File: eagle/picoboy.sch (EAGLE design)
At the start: 8 parts

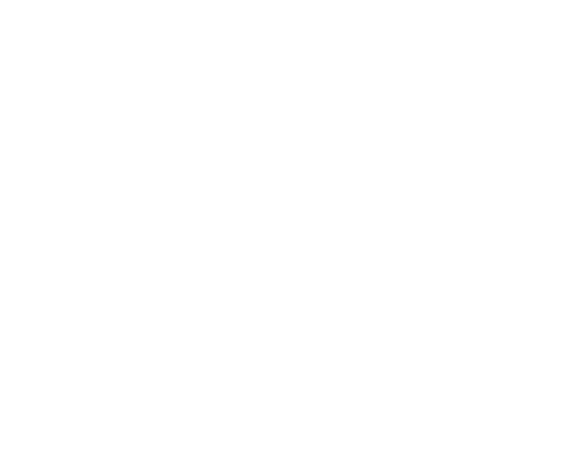
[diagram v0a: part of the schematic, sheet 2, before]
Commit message: Replace Game Boy Pocket with Game Boy Color PCB outline
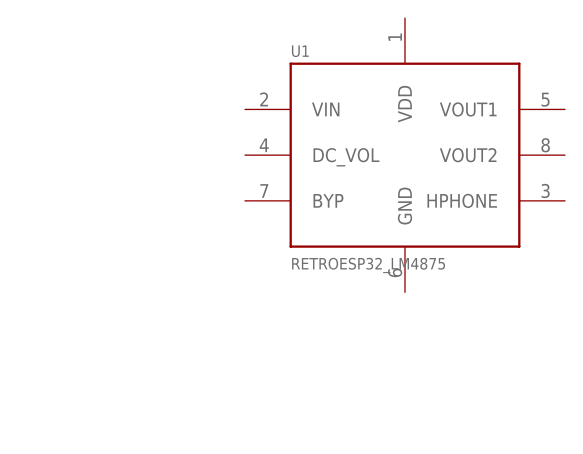
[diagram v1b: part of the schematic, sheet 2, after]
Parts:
- added U1: RETROESP32_LM4875, GabozeLite:RETROESP32_LM4875
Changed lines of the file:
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@@
 <part name="SELECT" library="GabozeLite" deviceset="RETROESP32_CONDUCTIVE_BUTTON_STARTSELECT" device="CONDUCTIVE_BUTTON_THICK_STARTSELECT"/>
 <part name="START" library="GabozeLite" deviceset="RETROESP32_CONDUCTIVE_BUTTON_STARTSELECT" device="CONDUCTIVE_BUTTON_THICK_STARTSELECT"/>
+<part name="U1" library="GabozeLite" deviceset="RETROESP32_LM4875" device=""/>
 </parts>
 <sheets>
@@
 <attribute name="NAME" x="76.2" y="151.13" size="1.9304" layer="95" font="vector" ratio="20" align="center"/>
 </instance>
+<instance part="U1" gate="U$1" x="182.88" y="162.56" smashed="yes">
+<attribute name="NAME" x="177.8" y="173.482" size="1.27" layer="95"/>
+<attribute name="VALUE" x="177.8" y="149.86" size="1.27" layer="96"/>
+</instance>
 </instances>

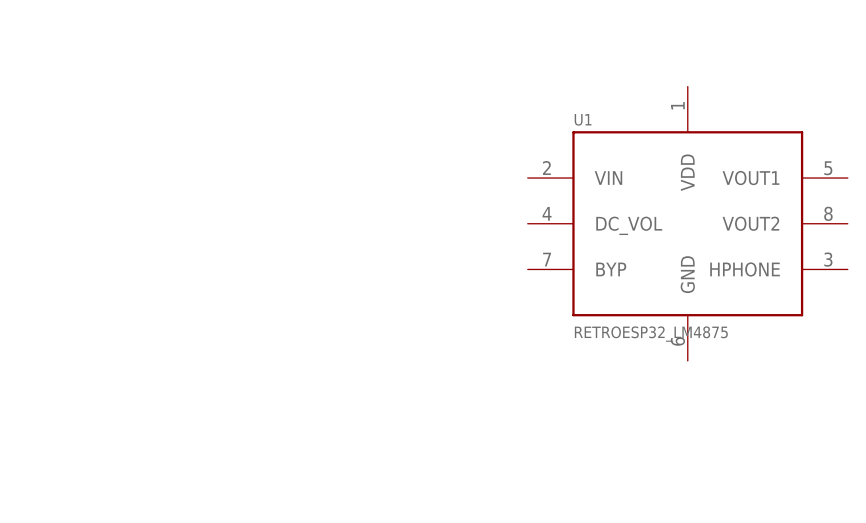
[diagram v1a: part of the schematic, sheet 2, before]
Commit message: Added devices to library
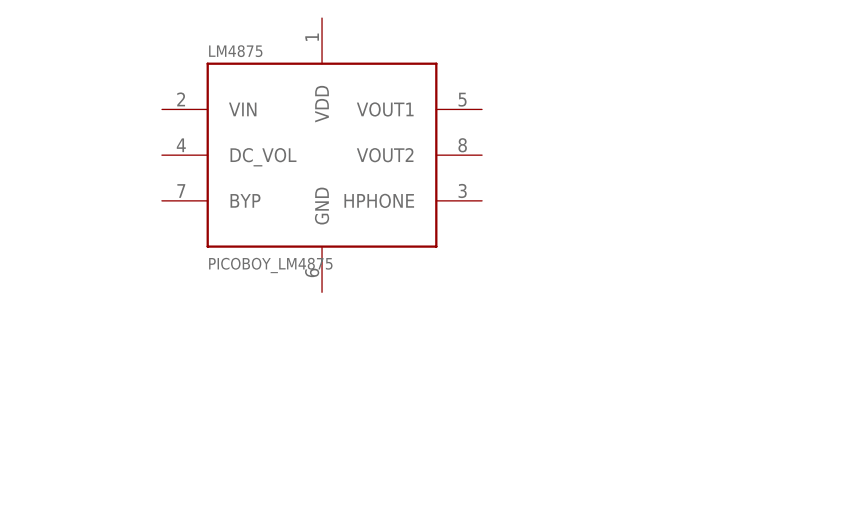
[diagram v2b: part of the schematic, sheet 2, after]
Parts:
- removed U1: RETROESP32_LM4875, GabozeLite:RETROESP32_LM4875
- added LM4875: PICOBOY_LM4875, picoboy:PICOBOY_LM4875
- A, B: value RETROESP32_CONDUCTIVE_BUTTONCONDUCTIVE_BUTTON_THICK -> PICOBOY_CONDUCTIVE_BUTTONCONDUCTIVE_BUTTON_THICK; device GabozeLite:RETROESP32_CONDUCTIVE_BUTTONCONDUCTIVE_BUTTON_THICK -> picoboy:PICOBOY_CONDUCTIVE_BUTTONCONDUCTIVE_BUTTON_THICK
- DOWN, LEFT, RIGHT, UP: value RETROESP32_CONDUCTIVE_BUTTONCONDUCTIVE_BUTTON_DIRECTIONAL_THICK -> PICOBOY_CONDUCTIVE_BUTTONCONDUCTIVE_BUTTON_DIRECTIONAL_THICK; device GabozeLite:RETROESP32_CONDUCTIVE_BUTTONCONDUCTIVE_BUTTON_DIRECTIONAL_THICK -> picoboy:PICOBOY_CONDUCTIVE_BUTTONCONDUCTIVE_BUTTON_DIRECTIONAL_THICK
- SELECT, START: value RETROESP32_CONDUCTIVE_BUTTON_STARTSELECTCONDUCTIVE_BUTTON_THICK_STARTSELECT -> PICOBOY_CONDUCTIVE_BUTTON_STARTSELECTCONDUCTIVE_BUTTON_THICK_STARTSELECT; device GabozeLite:RETROESP32_CONDUCTIVE_BUTTON_STARTSELECTCONDUCTIVE_BUTTON_THICK_STARTSELECT -> picoboy:PICOBOY_CONDUCTIVE_BUTTON_STARTSELECTCONDUCTIVE_BUTTON_THICK_STARTSELECT
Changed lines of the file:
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@@
 <parts>
 <part name="FRAME1" library="frames" library_urn="urn:adsk.eagle:library:229" deviceset="FRAME_A_L" device=""/>
-<part name="UP" library="GabozeLite" deviceset="RETROESP32_CONDUCTIVE_BUTTON" device="CONDUCTIVE_BUTTON_DIRECTIONAL_THICK"/>
-<part name="RIGHT" library="GabozeLite" deviceset="RETROESP32_CONDUCTIVE_BUTTON" device="CONDUCTIVE_BUTTON_DIRECTIONAL_THICK"/>
-<part name="DOWN" library="GabozeLite" deviceset="RETROESP32_CONDUCTIVE_BUTTON" device="CONDUCTIVE_BUTTON_DIRECTIONAL_THICK"/>
-<part name="LEFT" library="GabozeLite" deviceset="RETROESP32_CONDUCTIVE_BUTTON" device="CONDUCTIVE_BUTTON_DIRECTIONAL_THICK"/>
+<part name="UP" library="picoboy" deviceset="PICOBOY_CONDUCTIVE_BUTTON" device="CONDUCTIVE_BUTTON_DIRECTIONAL_THICK"/>
+<part name="RIGHT" library="picoboy" deviceset="PICOBOY_CONDUCTIVE_BUTTON" device="CONDUCTIVE_BUTTON_DIRECTIONAL_THICK"/>
+<part name="DOWN" library="picoboy" deviceset="PICOBOY_CONDUCTIVE_BUTTON" device="CONDUCTIVE_BUTTON_DIRECTIONAL_THICK"/>
+<part name="LEFT" library="picoboy" deviceset="PICOBOY_CONDUCTIVE_BUTTON" device="CONDUCTIVE_BUTTON_DIRECTIONAL_THICK"/>
 <part name="FRAME2" library="frames" library_urn="urn:adsk.eagle:library:229" deviceset="FRAME_A_L" device=""/>
-<part name="B" library="GabozeLite" deviceset="RETROESP32_CONDUCTIVE_BUTTON" device="CONDUCTIVE_BUTTON_THICK"/>
-<part name="A" library="GabozeLite" deviceset="RETROESP32_CONDUCTIVE_BUTTON" device="CONDUCTIVE_BUTTON_THICK"/>
-<part name="SELECT" library="GabozeLite" deviceset="RETROESP32_CONDUCTIVE_BUTTON_STARTSELECT" device="CONDUCTIVE_BUTTON_THICK_STARTSELECT"/>
-<part name="START" library="GabozeLite" deviceset="RETROESP32_CONDUCTIVE_BUTTON_STARTSELECT" device="CONDUCTIVE_BUTTON_THICK_STARTSELECT"/>
-<part name="U1" library="GabozeLite" deviceset="RETROESP32_LM4875" device=""/>
+<part name="B" library="picoboy" deviceset="PICOBOY_CONDUCTIVE_BUTTON" device="CONDUCTIVE_BUTTON_THICK"/>
+<part name="A" library="picoboy" deviceset="PICOBOY_CONDUCTIVE_BUTTON" device="CONDUCTIVE_BUTTON_THICK"/>
+<part name="SELECT" library="picoboy" deviceset="PICOBOY_CONDUCTIVE_BUTTON_STARTSELECT" device="CONDUCTIVE_BUTTON_THICK_STARTSELECT"/>
+<part name="START" library="picoboy" deviceset="PICOBOY_CONDUCTIVE_BUTTON_STARTSELECT" device="CONDUCTIVE_BUTTON_THICK_STARTSELECT"/>
+<part name="LM4875" library="picoboy" deviceset="PICOBOY_LM4875" device=""/>
 </parts>
 <sheets>
@@
 <attribute name="NAME" x="76.2" y="151.13" size="1.9304" layer="95" font="vector" ratio="20" align="center"/>
 </instance>
-<instance part="U1" gate="U$1" x="182.88" y="162.56" smashed="yes">
-<attribute name="NAME" x="177.8" y="173.482" size="1.27" layer="95"/>
-<attribute name="VALUE" x="177.8" y="149.86" size="1.27" layer="96"/>
+<instance part="LM4875" gate="U$1" x="142.24" y="170.18" smashed="yes">
+<attribute name="NAME" x="137.16" y="181.102" size="1.27" layer="95"/>
+<attribute name="VALUE" x="137.16" y="157.48" size="1.27" layer="96"/>
 </instance>
 </instances>
